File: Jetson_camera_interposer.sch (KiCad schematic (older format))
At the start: 20 parts, among them J1 QSH-060-01-L-D-A, J2 QTH-060-01-L-D-A, J21 Conn_01x01, J22 Conn_01x01, J23 Conn_01x01, J24 Conn_01x01, J25 Conn_01x01, J26 Conn_01x01, J3 Conn_01x01, J4 Conn_01x01, J5 Conn_01x01, J6 Conn_01x01, J7 Conn_02x10_Odd_Even, J8 Conn_02x30_Odd_Even

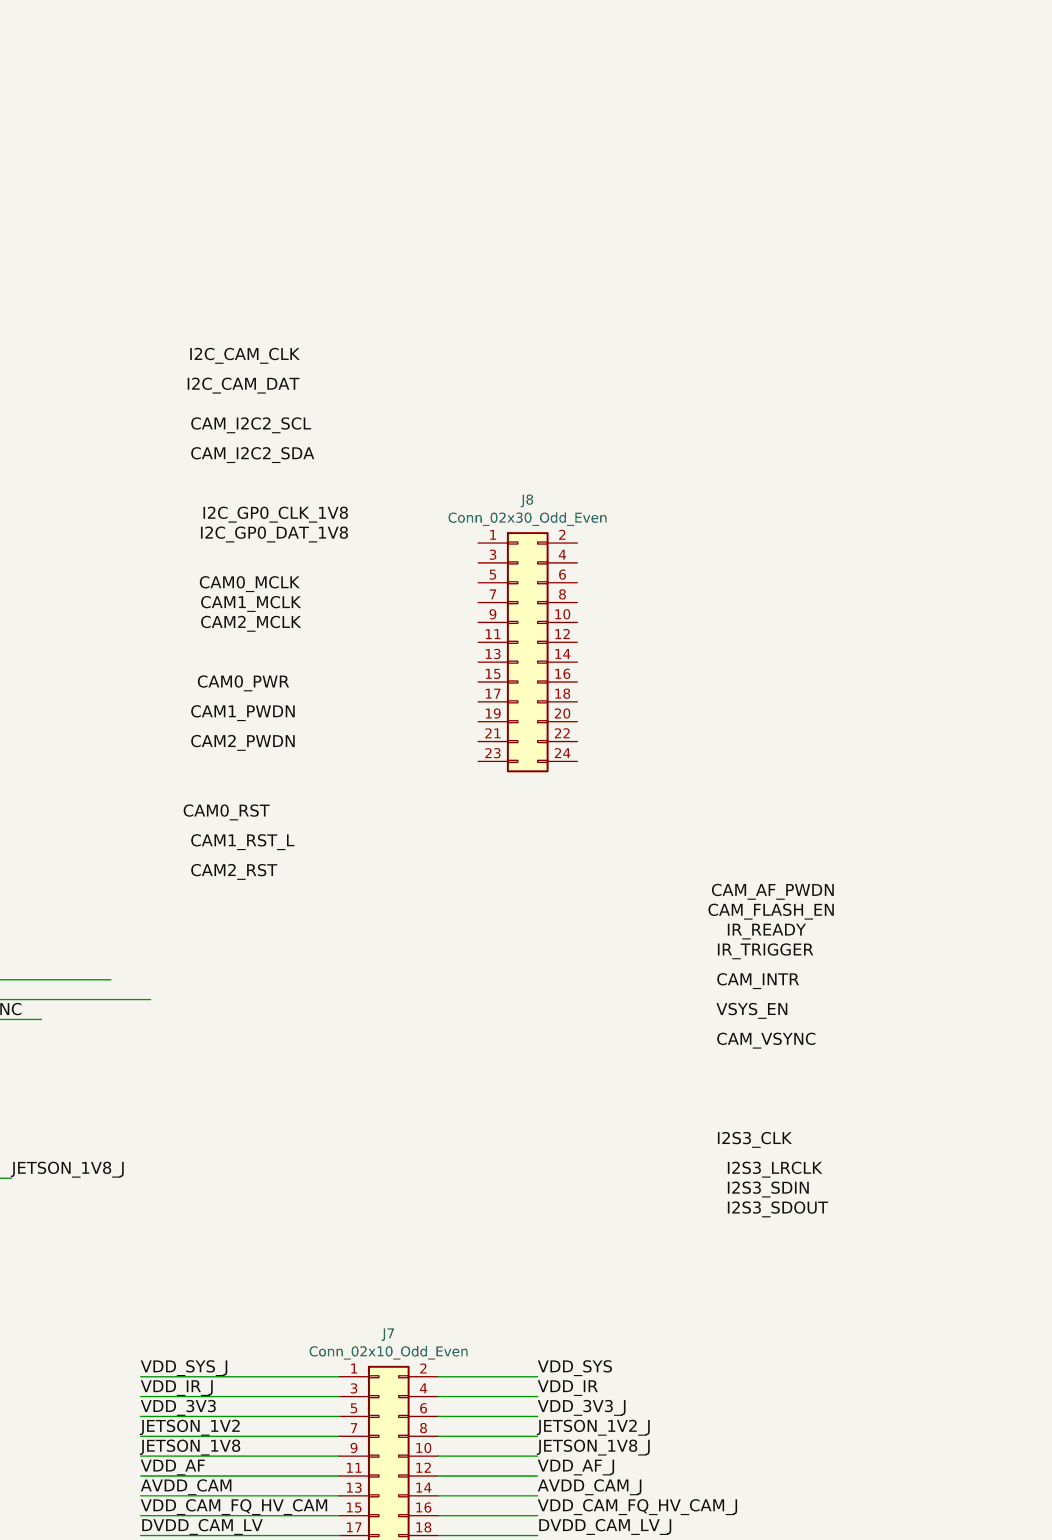
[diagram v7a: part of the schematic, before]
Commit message: organized footprints
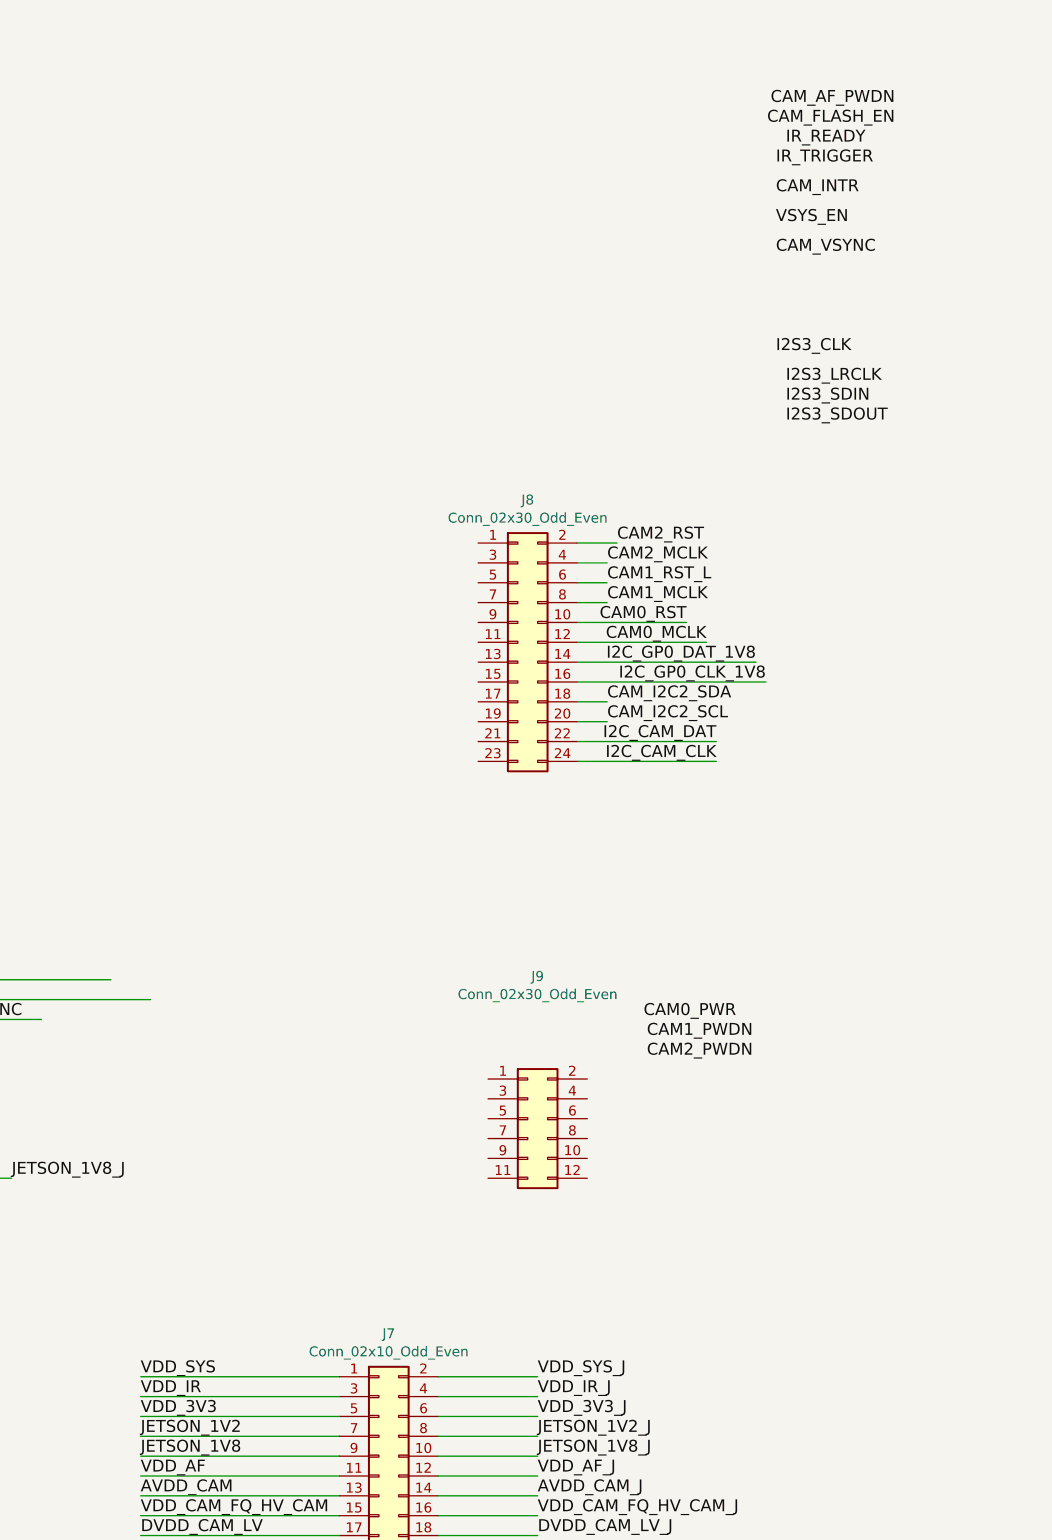
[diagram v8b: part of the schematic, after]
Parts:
- added J9: Conn_02x30_Odd_Even, Pin_Headers:Pin_Header_Straight_2x06_Pitch2.54mm, symbol Connector_Generic:Conn_02x06_Odd_Even
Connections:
- wire segments 331 -> 343
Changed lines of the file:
@@
 $EndComp
-Wire Wire Line
-	12850 7900 11850 7900
-Wire Wire Line
-	12850 8000 11850 8000
 Wire Wire Line
 	12850 8100 11850 8100
@@
 Wire Wire Line
 	13350 8100 13850 8100
-Wire Wire Line
-	13350 8000 13850 8000
-Wire Wire Line
-	13350 7900 13850 7900
-Text Label 11850 7900 0    60   ~ 0
+Text Label 13850 7900 0    60   ~ 0
 VDD_SYS_J
-Text Label 11850 8000 0    60   ~ 0
+Text Label 13850 8000 0    60   ~ 0
 VDD_IR_J
 Text Label 11850 8100 0    60   ~ 0
@@
 Wire Wire Line
 	13850 8800 13850 8950
-Text Label 13850 7900 0    60   ~ 0
+Text Label 11850 7900 0    60   ~ 0
 VDD_SYS
-Text Label 13850 8000 0    60   ~ 0
+Text Label 11850 8000 0    60   ~ 0
 VDD_IR
 Text Label 13850 8100 0    60   ~ 0
@@
 Wire Wire Line
 	9800 7700 10200 7700
-Text Label 12650 2800 2    60   ~ 0
+Text Label 14750 4800 2    60   ~ 0
 I2C_CAM_CLK
-Text Label 12650 2950 2    60   ~ 0
+Text Label 14750 4700 2    60   ~ 0
 I2C_CAM_DAT
-Text Label 15350 5500 2    60   ~ 0
+Text Label 15650 1500 2    60   ~ 0
 CAM_AF_PWDN
-Text Label 12100 3150 0    60   ~ 0
-CAM_I2C2_SCL
-Text Label 12100 3300 0    60   ~ 0
-CAM_I2C2_SDA
-Text Label 12650 3950 2    60   ~ 0
+Text Label 14700 4200 2    60   ~ 0
 CAM0_MCLK
-Text Label 12600 4450 2    60   ~ 0
+Text Label 14850 6100 2    60   ~ 0
 CAM0_PWR
-Text Label 15350 5600 2    60   ~ 0
+Text Label 15650 1600 2    60   ~ 0
 CAM_FLASH_EN
-Text Label 12900 3600 2    60   ~ 0
-I2C_GP0_CLK_1V8
-Text Label 12900 3700 2    60   ~ 0
-I2C_GP0_DAT_1V8
-Text Label 14800 5700 0    60   ~ 0
+Text Label 15100 1700 0    60   ~ 0
 IR_READY
-Text Label 14750 5800 0    60   ~ 0
+Text Label 15050 1800 0    60   ~ 0
 IR_TRIGGER
-Text Label 14750 5950 0    60   ~ 0
+Text Label 15050 1950 0    60   ~ 0
 CAM_INTR
-Text Label 14750 6100 0    60   ~ 0
+Text Label 15050 2100 0    60   ~ 0
 VSYS_EN
-Text Label 14750 6750 0    60   ~ 0
+Text Label 15050 2750 0    60   ~ 0
 I2S3_CLK
-Text Label 14800 6900 0    60   ~ 0
+Text Label 15100 2900 0    60   ~ 0
 I2S3_LRCLK
-Text Label 14800 7000 0    60   ~ 0
+Text Label 15100 3000 0    60   ~ 0
 I2S3_SDIN
-Text Label 14800 7100 0    60   ~ 0
+Text Label 15100 3100 0    60   ~ 0
 I2S3_SDOUT
-Text Label 14750 6250 0    60   ~ 0
+Text Label 15050 2250 0    60   ~ 0
 CAM_VSYNC
-Text Label 12150 4050 0    60   ~ 0
+Text Label 14200 4000 0    60   ~ 0
 CAM1_MCLK
-Text Label 12100 4600 0    60   ~ 0
+Text Label 14400 6200 0    60   ~ 0
 CAM1_PWDN
-Text Label 12100 5250 0    60   ~ 0
-CAM1_RST_L
-Text Label 12150 4150 0    60   ~ 0
+Text Label 14200 3800 0    60   ~ 0
 CAM2_MCLK
-Text Label 12100 4750 0    60   ~ 0
+Text Label 14400 6300 0    60   ~ 0
 CAM2_PWDN
-Text Label 12100 5400 0    60   ~ 0
+Text Label 14250 3700 0    60   ~ 0
 CAM2_RST
-Text Label 12500 5100 2    60   ~ 0
+Text Label 14600 4100 2    60   ~ 0
 CAM0_RST
 $Comp
@@
 	1    0    0    -1
 $EndComp
+Wire Wire Line
+	12850 7900 11850 7900
+Wire Wire Line
+	12850 8000 11850 8000
+Wire Wire Line
+	13350 7900 13850 7900
+Wire Wire Line
+	13350 8000 13850 8000
+Text Label 14200 3900 0    60   ~ 0
+CAM1_RST_L
+$Comp
+L Connector_Generic:Conn_02x06_Odd_Even J9
+U 1 1 61A4E08F
+P 13800 6600
+F 0 "J9" H 13850 7317 50  0000 C CNN
+F 1 "Conn_02x30_Odd_Even" H 13850 7226 50  0000 C CNN
+F 2 "Pin_Headers:Pin_Header_Straight_2x06_Pitch2.54mm" H 13800 6600 50  0001 C CNN
+F 3 "~" H 13800 6600 50  0001 C CNN
+	1    13800 6600
+	1    0    0    -1
+$EndComp
+Text Label 14950 4300 2    60   ~ 0
+I2C_GP0_DAT_1V8
+Text Label 15000 4400 2    60   ~ 0
+I2C_GP0_CLK_1V8
+Text Label 14200 4600 0    60   ~ 0
+CAM_I2C2_SCL
+Text Label 14200 4500 0    60   ~ 0
+CAM_I2C2_SDA
+Wire Wire Line
+	14050 3900 14200 3900
+Wire Wire Line
+	14050 4000 14200 4000
+Wire Wire Line
+	14050 4300 14950 4300
+Wire Wire Line
+	14050 4400 15000 4400
+Wire Wire Line
+	14050 4500 14200 4500
+Wire Wire Line
+	14050 4600 14200 4600
+Wire Wire Line
+	14050 4700 14750 4700
+Wire Wire Line
+	14050 4800 14750 4800
+Wire Wire Line
+	14050 3700 14250 3700
+Wire Wire Line
+	14050 3800 14200 3800
+Wire Wire Line
+	14050 4100 14600 4100
+Wire Wire Line
+	14050 4200 14700 4200
 $EndSCHEMATC
